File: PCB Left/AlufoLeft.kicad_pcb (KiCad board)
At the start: 2 copper layers, 139.7 x 90.9 mm, 67 parts, among them J1 USB_C_Receptacle_USB2.0_16P_2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, J3 USB_C_Receptacle_USB2.0_16P_2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, J5 Shield_Connection, J7 Shield_Connection, J9 Shield_Connection, K11 PG1350, K12 PG1350, K13 PG1350, K14 PG1350, K15 PG1350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

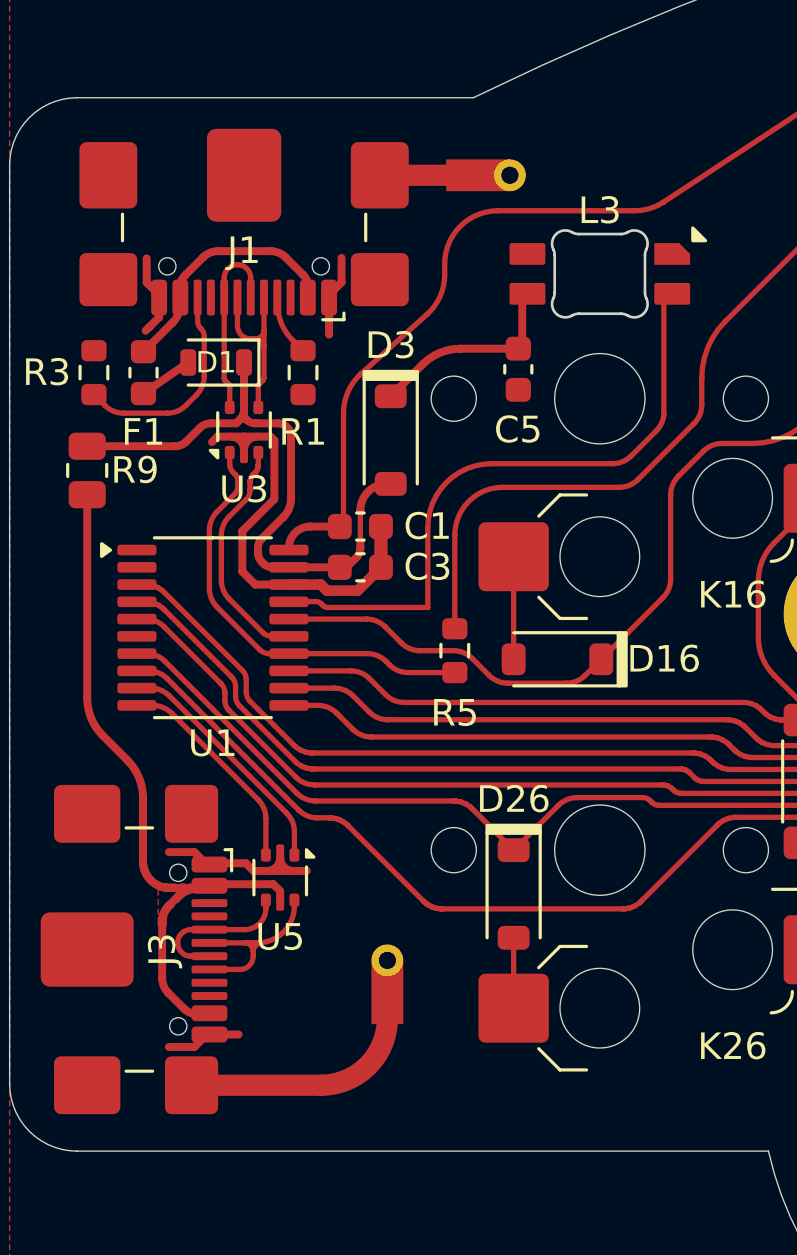
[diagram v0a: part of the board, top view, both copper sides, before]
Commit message: Tweak positioning of shield connections
Should now be the same on each side and align with other elements.
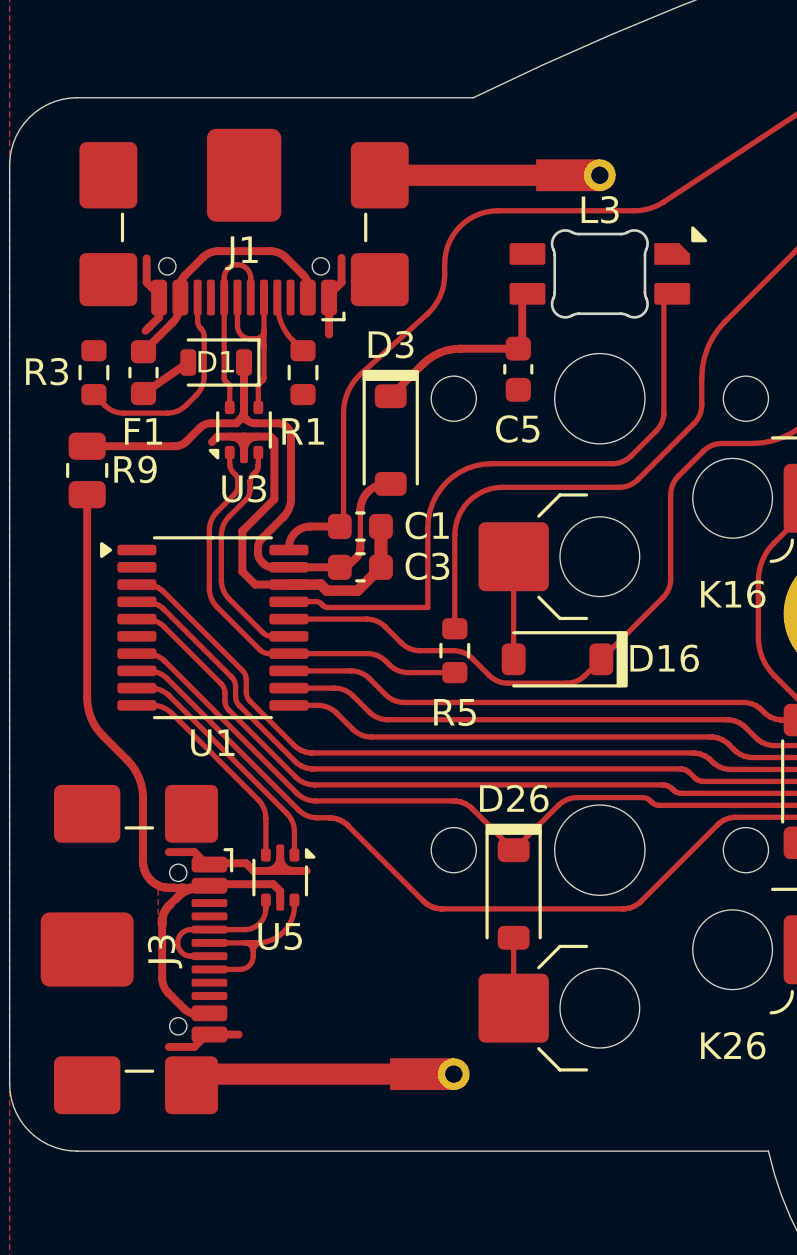
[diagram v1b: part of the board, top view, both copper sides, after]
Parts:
- moved J7 3.74 mm to (184.1, 77.9), turned to 90 degrees
- moved J5 3.39 mm to (189.6, 44.0)
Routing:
- net Net-(J5-Pin_1): track 3.70 -> 7.09 mm
- net Net-(J7-Pin_1): track 9.70 -> 8.85 mm
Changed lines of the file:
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@@
 		(tenting front back)
 		(pcbplotparams
-			(layerselection 0x00000000_00000000_55d57f55_57555550)
+			(layerselection 0x00000000_00000000_55d5ff55_57555550)
 			(plot_on_all_layers_selection 0x00000000_00000000_00000000_00000000)
 			(disableapertmacros no)
@@
 	(footprint "Project_Library:Shield_Connector"
 		(layer "F.Cu")
-		(at 182.499 74.466683 180)
+		(at 184.1 77.851 90)
 		(descr "Wire connection from PCB to aluminum core")
 		(property "Reference" "J7"
-			(at 0 -0.499999 180)
+			(at 0 -0.499999 90)
 			(unlocked yes)
 			(layer "F.SilkS")
@@
 		)
 		(property "Value" "Shield_Connection"
-			(at 0 1 180)
+			(at 0 1 90)
 			(unlocked yes)
 			(layer "F.Fab")
@@
 		)
 		(property "Datasheet" ""
-			(at 0 0 180)
+			(at 0 0 90)
 			(unlocked yes)
 			(layer "F.Fab")
@@
 		)
 		(property "Description" "Generic connector, single row, 01x01, script generated (kicad-library-utils/schlib/autogen/connector/)"
-			(at 0 0 180)
+			(at 0 0 90)
 			(unlocked yes)
 			(layer "F.Fab")
@@
 		)
 		(fp_text user "${REFERENCE}"
-			(at 0 2.5 180)
+			(at 0 2.5 90)
 			(unlocked yes)
 			(layer "F.Fab")
@@
 		)
 		(pad "1" smd roundrect
-			(at 0 -0.3 180)
+			(at 0 -0.3 90)
 			(size 1.2 2.4)
 			(layers "F.Cu" "F.Mask" "F.Paste")
@@
 		)
 		(pad "1" thru_hole circle
-			(at 0 0.9 180)
+			(at 0 0.9 90)
 			(size 1.2 1.2)
 			(drill 0.65)
@@
 	(footprint "Project_Library:Shield_Connector"
 		(layer "F.Cu")
-		(at 186.2145 44.003 90)
+		(at 189.6 44.003 90)
 		(descr "Wire connection from PCB to aluminum core")
 		(property "Reference" "J5"
@@
 	(segment
 		(start 182.2145 44.003)
-		(end 185.9145 44.003)
+		(end 189.3 44.003)
 		(width 0.8)
 		(layer "F.Cu")
@@
 	(segment
 		(start 175.125 78.268684)
-		(end 179.999 78.268684)
+		(end 175.542684 77.851)
 		(width 0.8)
 		(layer "F.Cu")
@@
 	)
 	(segment
-		(start 182.499 75.768684)
-		(end 182.499 74.766683)
-		(width 0.8)
-		(layer "F.Cu")
-		(net 67)
-	)
-	(arc
-		(start 179.999 78.268684)
-		(mid 181.766767 77.536451)
-		(end 182.499 75.768684)
+		(start 175.542684 77.851)
+		(end 183.8 77.851)
 		(width 0.8)
 		(layer "F.Cu")

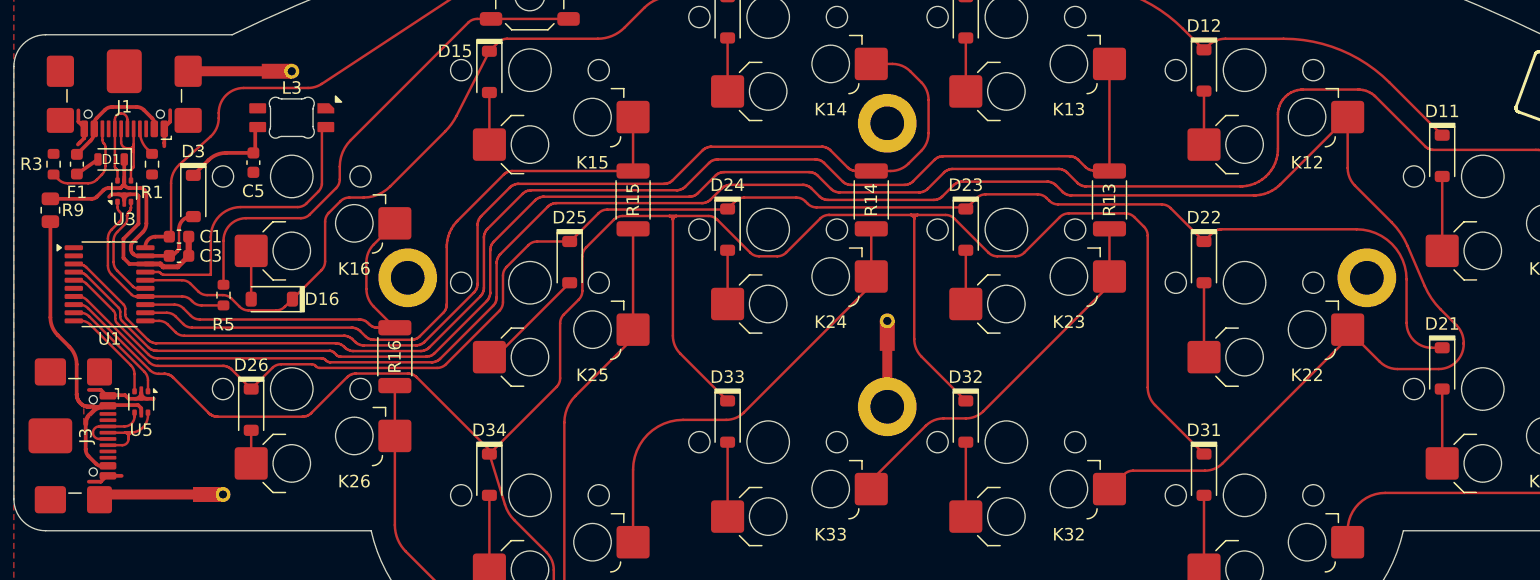
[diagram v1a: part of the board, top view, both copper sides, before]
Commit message: Minor tweaks
 * Relocate lefthand 5V decoupling capacitor
 * Alter spoke rotation on USB port A1 and A12 pads (this gives more ground connections when combined with B1 and B12)
 * Routing improvements
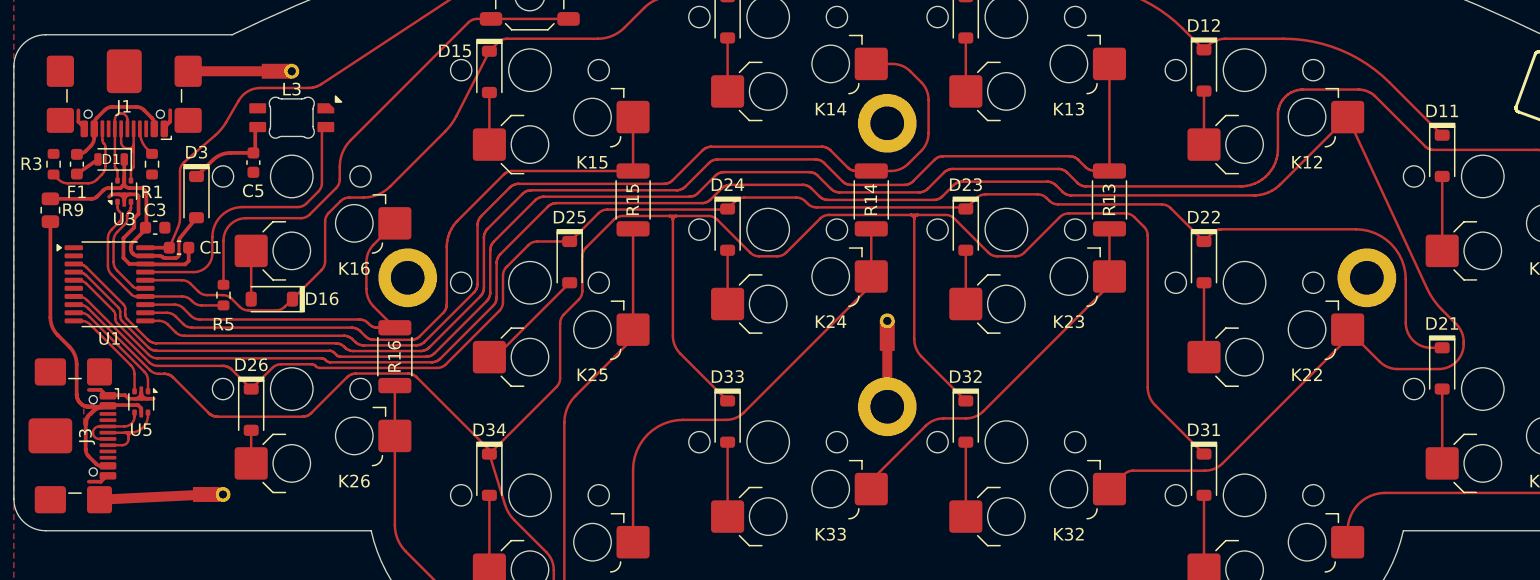
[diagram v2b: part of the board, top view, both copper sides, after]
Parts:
- moved C3 2.95 mm to (179.6, 56.5)
- moved C1 0.88 mm to (181.5, 58.1)
- moved D3 0.27 mm to (182.9, 54.1)
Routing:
- net GND: track 25.5 -> 20.4 mm
- net LED: track 24.0 -> 23.0 mm
- net Col2: track 172.7 -> 172.0 mm
